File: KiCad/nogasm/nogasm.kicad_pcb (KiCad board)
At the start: 4 copper layers, 80 x 80 mm, 80 parts, among them J1 Barrel_Jack, J2 AudioJack4, J3 USB_B_Micro, Q1 AP55N03K, SW1 SW_Push, SW2 Rotary_Encoder_Switch, SW3 SW_DIP_x04, SW4 SW_DIP_x01, U1 MPXV5100DP, U2 LD29150DT50R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

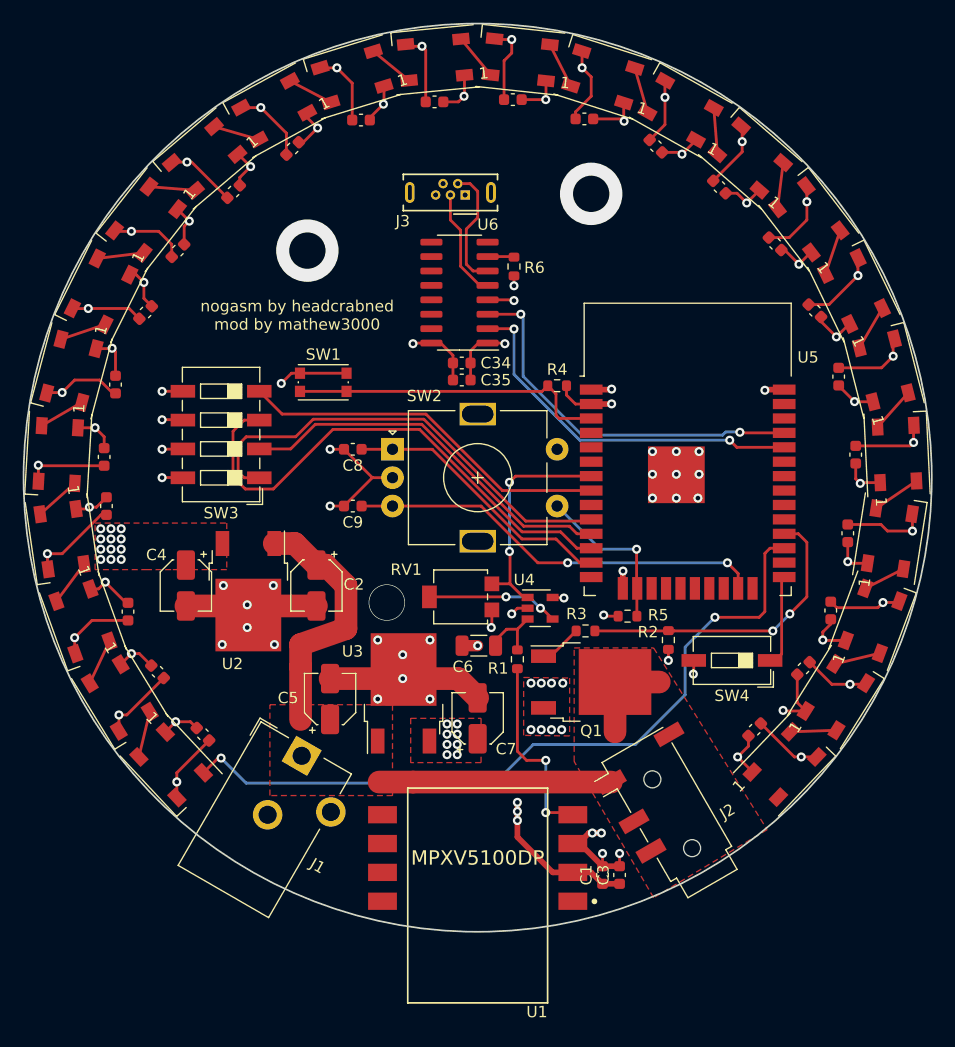
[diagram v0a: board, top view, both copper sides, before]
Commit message: Added Autoflash for ESP32 and Center-LED
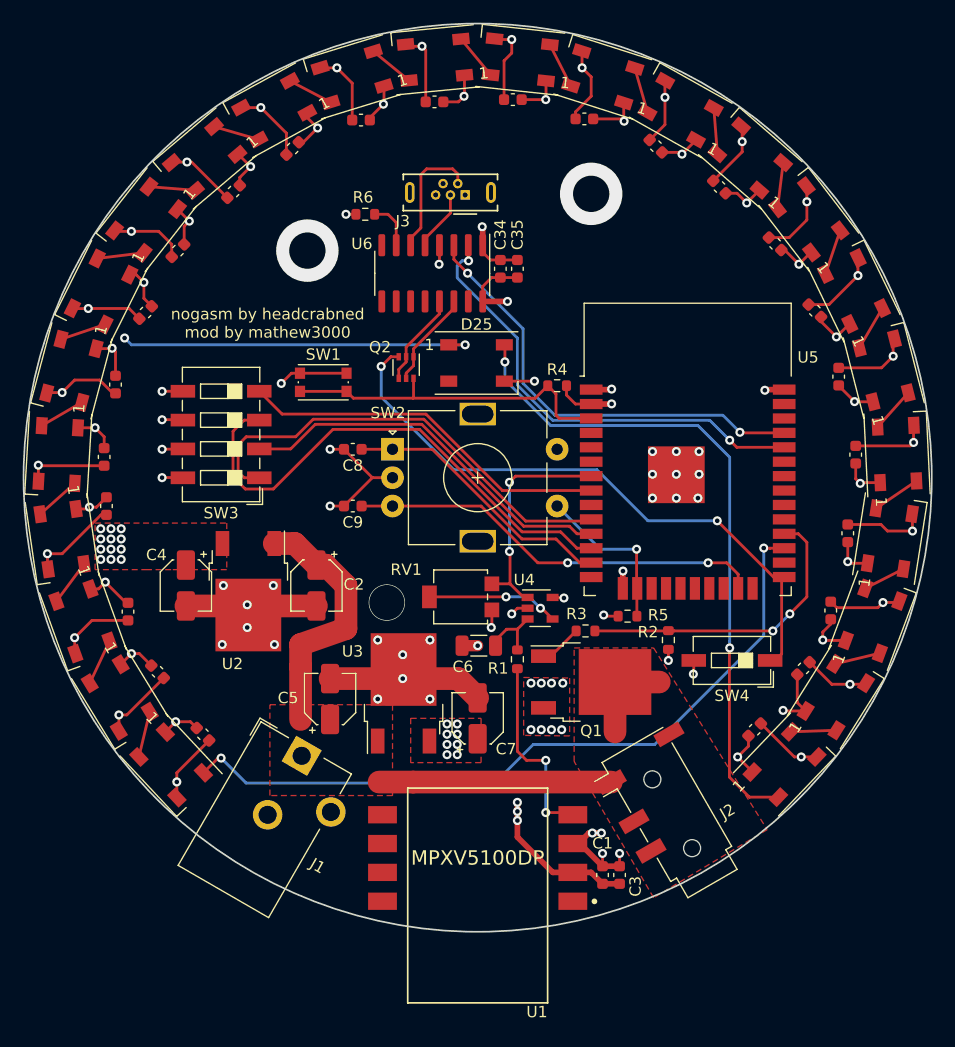
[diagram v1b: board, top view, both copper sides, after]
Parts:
- added D25: WS2812B, LED_SMD:LED_WS2812B_PLCC4_5.0x5.0mm_P3.2mm, F.Cu at (139.9, 79.9)
- added Q2: UMH3N, Package_TO_SOT_SMD:SOT-363_SC-70-6, F.Cu at (133.7, 80.3)
- moved R6 13.9 mm to (130.1, 66.8), turned to 180 degrees
- moved C35 11.0 mm to (143.5, 71.6), turned to 90 degrees
- moved C34 8.97 mm to (142.0, 71.6), turned to 90 degrees
- moved U6 2.94 mm to (136.0, 72.0), turned to 270 degrees
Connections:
- U6 pad 13: Net-(U6-Pad13) -> /DTR
- U6 pad 14: Net-(U6-Pad14) -> /RTS
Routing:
- net /LEDS/Data-Out: track 0.00 -> 59.0 mm, vias 0 -> 2
- net /IO0: track 8.11 -> 54.8 mm, vias 0 -> 2
- net +5V: track 92.4 -> 124.1 mm, vias 36 -> 38
- net /RTS: track 0.00 -> 8.52 mm
- net /RX_ESP: track 32.8 -> 41.2 mm
- net /DTR: track 0.00 -> 8.26 mm
- net /TX_ESP: track 33.8 -> 39.5 mm
- net Net-(J3-Pad3): track 9.73 -> 5.35 mm
- net GND: track 235.1 -> 237.5 mm, vias 73 -> 74
- net /EN: track 28.2 -> 30.4 mm
- net Net-(R6-Pad1): track 2.35 -> 4.20 mm
- net /LED: track 66.6 -> 65.9 mm

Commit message: Updated to new KicadFormat
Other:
- net class Default removed

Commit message: Updated pcb layout and 3d model
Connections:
- D25 pad 2: Net-(D25-Pad2) -> unconnected-(D25-Pad2)
- J3 pad 1: Net-(J3-Pad1) -> unconnected-(J3-Pad1)
- J3 pad 4: Net-(J3-Pad4) -> unconnected-(J3-Pad4)
- U1 pad 1: Net-(U1-Pad1) -> unconnected-(U1-Pad1)
- U1 pad 5: Net-(U1-Pad5) -> unconnected-(U1-Pad5)
- U1 pad 6: Net-(U1-Pad6) -> unconnected-(U1-Pad6)
- U1 pad 7: Net-(U1-Pad7) -> unconnected-(U1-Pad7)
- U1 pad 8: Net-(U1-Pad8) -> unconnected-(U1-Pad8)
- U5 pad 14: Net-(U5-Pad14) -> unconnected-(U5-Pad14)
- U5 pad 17: Net-(U5-Pad17) -> unconnected-(U5-Pad17)
- U5 pad 18: Net-(U5-Pad18) -> unconnected-(U5-Pad18)
- U5 pad 19: Net-(U5-Pad19) -> unconnected-(U5-Pad19)
- U5 pad 20: Net-(U5-Pad20) -> unconnected-(U5-Pad20)
- U5 pad 21: Net-(U5-Pad21) -> unconnected-(U5-Pad21)
- U5 pad 22: Net-(U5-Pad22) -> unconnected-(U5-Pad22)
- U5 pad 24: Net-(U5-Pad24) -> unconnected-(U5-Pad24)
- U5 pad 26: Net-(U5-Pad26) -> unconnected-(U5-Pad26)
- U5 pad 29: Net-(U5-Pad29) -> unconnected-(U5-Pad29)
- U5 pad 30: Net-(U5-Pad30) -> unconnected-(U5-Pad30)
- U5 pad 31: Net-(U5-Pad31) -> unconnected-(U5-Pad31)
- U5 pad 32: Net-(U5-Pad32) -> unconnected-(U5-Pad32)
- U5 pad 33: Net-(U5-Pad33) -> unconnected-(U5-Pad33)
- U5 pad 36: Net-(U5-Pad36) -> unconnected-(U5-Pad36)
- U5 pad 37: Net-(U5-Pad37) -> unconnected-(U5-Pad37)
- U5 pad 4: Net-(U5-Pad4) -> unconnected-(U5-Pad4)
- U5 pad 5: Net-(U5-Pad5) -> unconnected-(U5-Pad5)
- U5 pad 6: Net-(U5-Pad6) -> unconnected-(U5-Pad6)
- U5 pad 9: Net-(U5-Pad9) -> unconnected-(U5-Pad9)
- U6 pad 10: Net-(U6-Pad10) -> unconnected-(U6-Pad10)
- U6 pad 11: Net-(U6-Pad11) -> unconnected-(U6-Pad11)
- U6 pad 12: Net-(U6-Pad12) -> unconnected-(U6-Pad12)
- U6 pad 15: Net-(U6-Pad15) -> unconnected-(U6-Pad15)
- U6 pad 8: Net-(U6-Pad8) -> unconnected-(U6-Pad8)
- U6 pad 9: Net-(U6-Pad9) -> unconnected-(U6-Pad9)

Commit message: fixed missing ground and vcc for 2 leds because of esp keepout
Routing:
- net +5V: track 124.1 -> 125.0 mm
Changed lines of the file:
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@@
   (segment (start 124.4 106.649374) (end 124.4 111.3) (width 2) (layer "F.Cu") (net 3))
   (segment (start 134.312453 116.812453) (end 131.312453 116.812453) (width 2) (layer "F.Cu") (net 3))
+  (segment (start 172.777872 75.272128) (end 173.1 74.95) (width 0.25) (layer "F.Cu") (net 4))
   (segment (start 130.5 58.3) (end 131.7 57.1) (width 0.25) (layer "F.Cu") (net 4))
   (segment (start 119.048008 64.251992) (end 119.048008 63.551992) (width 0.25) (layer "F.Cu") (net 4))
   (segment (start 161.848008 64.948008) (end 162.848008 64.948008) (width 0.25) (layer "F.Cu") (net 4))
-  (segment (start 170.248008 76.248008) (end 171.6 77.6) (width 0.25) (layer "F.Cu") (net 4))
   (segment (start 136.975 56.9) (end 138.3 56.9) (width 0.25) (layer "F.Cu") (net 4))
   (segment (start 170.4 103.6) (end 170.4 104.3) (width 0.25) (layer "F.Cu") (net 4))
+  (segment (start 172.013506 75.85) (end 171.086494 75.85) (width 0.25) (layer "F.Cu") (net 4))
   (segment (start 110.6 74.207968) (end 111.296016 74.903984) (width 0.25) (layer "F.Cu") (net 4))
-  (segment (start 167.048008 69.948008) (end 168.3 71.2) (width 0.25) (layer "F.Cu") (net 4))
   (segment (start 168.151992 107.348008) (end 168.151992 109.810525) (width 0.25) (layer "F.Cu") (net 4))
   (segment (start 170.248008 75.848008) (end 170.248008 76.248008) (width 0.25) (layer "F.Cu") (net 4))
@@
   (segment (start 109.35708 72.121327) (end 109.921327 72.121327) (width 0.25) (layer "F.Cu") (net 4))
   (segment (start 166.952211 110.552211) (end 166.9 110.5) (width 0.25) (layer "F.Cu") (net 4))
+  (segment (start 170.286494 75.85) (end 171.213506 75.85) (width 0.25) (layer "F.Cu") (net 4))
+  (segment (start 169.02498 69.62498) (end 169.3971 69.62498) (width 0.25) (layer "F.Cu") (net 4))
   (segment (start 143.875 56.7) (end 146 56.7) (width 0.25) (layer "F.Cu") (net 4))
   (segment (start 119.048008 63.551992) (end 120 62.6) (width 0.25) (layer "F.Cu") (net 4))
@@
   (segment (start 105.8 92.6) (end 106.425 92.6) (width 0.25) (layer "F.Cu") (net 4))
   (segment (start 174.826722 83.314287) (end 173.214287 83.314287) (width 0.25) (layer "F.Cu") (net 4))
-  (segment (start 169.338266 70.161734) (end 168.3 71.2) (width 0.25) (layer "F.Cu") (net 4))
   (segment (start 156.248008 61.348008) (end 157.848008 61.348008) (width 0.25) (layer "F.Cu") (net 4))
   (segment (start 152.7 58.4) (end 152.9 58.6) (width 0.25) (layer "F.Cu") (net 4))
@@
   (segment (start 110.6 72.8) (end 110.6 74.207968) (width 0.25) (layer "F.Cu") (net 4))
   (segment (start 131.749157 55.50187) (end 131.749157 57.050843) (width 0.25) (layer "F.Cu") (net 4))
+  (segment (start 168.35 68.95) (end 169.02498 69.62498) (width 0.25) (layer "F.Cu") (net 4))
   (segment (start 108.1 81.025) (end 108.1 78.9) (width 0.25) (layer "F.Cu") (net 4))
   (segment (start 170.438515 104.338515) (end 170.4 104.3) (width 0.25) (layer "F.Cu") (net 4))
   (segment (start 124.648008 60.451992) (end 125.9 59.2) (width 0.25) (layer "F.Cu") (net 4))
+  (segment (start 172 75.85) (end 172.655496 76.505496) (width 0.25) (layer "F.Cu") (net 4))
   (segment (start 172.430316 104.338515) (end 170.438515 104.338515) (width 0.25) (layer "F.Cu") (net 4))
   (segment (start 114.148008 67.851992) (end 114.6 67.4) (width 0.25) (layer "F.Cu") (net 4))
@@
   (segment (start 106.292835 85.607165) (end 106.3 85.6) (width 0.25) (layer "F.Cu") (net 4))
   (segment (start 124.248008 60.451992) (end 124.648008 60.451992) (width 0.25) (layer "F.Cu") (net 4))
+  (segment (start 172.777872 76.462799) (end 172.777872 75.272128) (width 0.25) (layer "F.Cu") (net 4))
   (segment (start 106.600313 99.799687) (end 107.2 99.2) (width 0.25) (layer "F.Cu") (net 4))
+  (segment (start 167.67502 69.62498) (end 166.748008 69.62498) (width 0.25) (layer "F.Cu") (net 4))
   (segment (start 113.566834 66.340267) (end 113.566834 66.366834) (width 0.25) (layer "F.Cu") (net 4))
   (segment (start 152.865568 58.565568) (end 152.9 58.6) (width 0.25) (layer "F.Cu") (net 4))
-  (segment (start 172.737201 76.462799) (end 171.6 77.6) (width 0.25) (layer "F.Cu") (net 4))
   (segment (start 109.5 105.5) (end 110.2 105.5) (width 0.25) (layer "F.Cu") (net 4))
   (segment (start 110.2 105.5) (end 111.251992 106.551992) (width 0.25) (layer "F.Cu") (net 4))
@@
   (segment (start 107.2 99.2) (end 109.025 101.025) (width 0.25) (layer "F.Cu") (net 4))
   (segment (start 174.349224 97.540965) (end 172.740965 97.540965) (width 0.25) (layer "F.Cu") (net 4))
+  (segment (start 168.35 68.95) (end 167.67502 69.62498) (width 0.25) (layer "F.Cu") (net 4))
   (segment (start 171.1 102.475) (end 171.1 102.9) (width 0.25) (layer "F.Cu") (net 4))
   (segment (start 106.425 92.6) (end 107.3 91.725) (width 0.25) (layer "F.Cu") (net 4))
@@
   (via (at 107.7 96.3) (size 0.8) (drill 0.4) (layers "F.Cu" "B.Cu") (net 4))
   (via (at 131.7 57.1) (size 0.8) (drill 0.4) (layers "F.Cu" "B.Cu") (net 4))
+  (via (at 173.1 74.95) (size 0.8) (drill 0.4) (layers "F.Cu" "B.Cu") (free) (net 4))
   (via (at 108.6 95.4) (size 0.8) (drill 0.4) (layers "F.Cu" "B.Cu") (net 4))
   (via (at 120 62.6) (size 0.8) (drill 0.4) (layers "F.Cu" "B.Cu") (net 4))
@@
   (via (at 106.8 97.2) (size 0.8) (drill 0.4) (layers "F.Cu" "B.Cu") (net 4))
   (via (at 125.9 59.2) (size 0.8) (drill 0.4) (layers "F.Cu" "B.Cu") (net 4))
-  (via (at 171.6 77.6) (size 0.8) (drill 0.4) (layers "F.Cu" "B.Cu") (net 4))
   (via (at 108.9 77.7) (size 0.8) (drill 0.4) (layers "F.Cu" "B.Cu") (net 4))
   (via (at 107.8 78.6) (size 0.8) (drill 0.4) (layers "F.Cu" "B.Cu") (net 4))
-  (via (at 168.3 71.2) (size 0.8) (drill 0.4) (layers "F.Cu" "B.Cu") (net 4))
   (via (at 114.6 67.4) (size 0.8) (drill 0.4) (layers "F.Cu" "B.Cu") (net 4))
   (via (at 105.8 92.6) (size 0.8) (drill 0.4) (layers "F.Cu" "B.Cu") (net 4))
@@
   (via (at 172.6 97.4) (size 0.8) (drill 0.4) (layers "F.Cu" "B.Cu") (net 4))
   (via (at 173.7 90.5) (size 0.8) (drill 0.4) (layers "F.Cu" "B.Cu") (net 4))
+  (via (at 168.35 68.95) (size 0.8) (drill 0.4) (layers "F.Cu" "B.Cu") (free) (net 4))
   (via (at 107.7 94.5) (size 0.8) (drill 0.4) (layers "F.Cu" "B.Cu") (net 4))
   (via (at 108.6 97.2) (size 0.8) (drill 0.4) (layers "F.Cu" "B.Cu") (net 4))

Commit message: updated parts for jlc
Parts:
- C6: value 33uF -> 22uF

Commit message: updated parts for jlc
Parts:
- U6: value CH340B (wrong symbol) -> CH340C (wrong symbol)
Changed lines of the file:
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@@
     (descr "SOIC, 16 Pin (JEDEC MS-012AC, https://www.analog.com/media/en/package-pcb-resources/package/pkg_pdf/soic_narrow-r/r_16.pdf), generated with kicad-footprint-generator ipc_gullwing_generator.py")
     (tags "SOIC SO")
-    (property "LCSC" "C81010")
+    (property "LCSC" "C7464026")
     (property "Sheetfile" "nogasm.kicad_sch")
     (property "Sheetname" "")
@@
         (effects (font (size 1 1) (thickness 0.15)))
     )
-    (fp_text value "CH340B (wrong symbol)" (at 0 5.9 90) (layer "F.Fab")
+    (fp_text value "CH340C (wrong symbol)" (at 0 5.9 90) (layer "F.Fab")
         (effects (font (size 1 1) (thickness 0.15)))
     )
@@
     (descr "SOT-363, SC-70-6")
     (tags "SOT-363 SC-70-6")
+    (property "LCSC" "C62892")
     (property "Sheetfile" "nogasm.kicad_sch")
     (property "Sheetname" "")
